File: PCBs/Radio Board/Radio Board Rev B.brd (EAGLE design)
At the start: 95.9 x 90.2 mm, 18 parts, among them J1 MOLEX_504050-0491, J1_1 TPTP10SQ, J1_2 TPTP10SQ, J1_3 TPTP10SQ, J1_4 TPTP10SQ

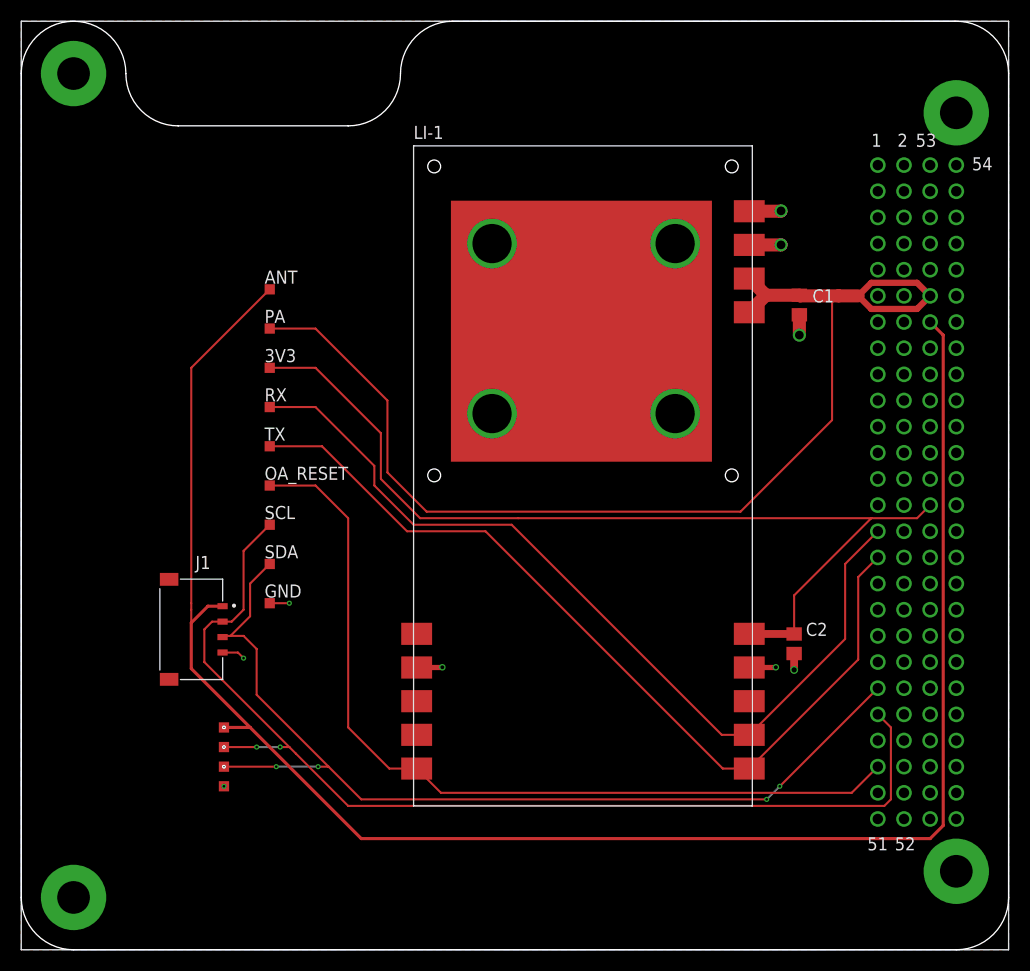
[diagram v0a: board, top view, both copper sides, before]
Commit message: Move MicroLock connector
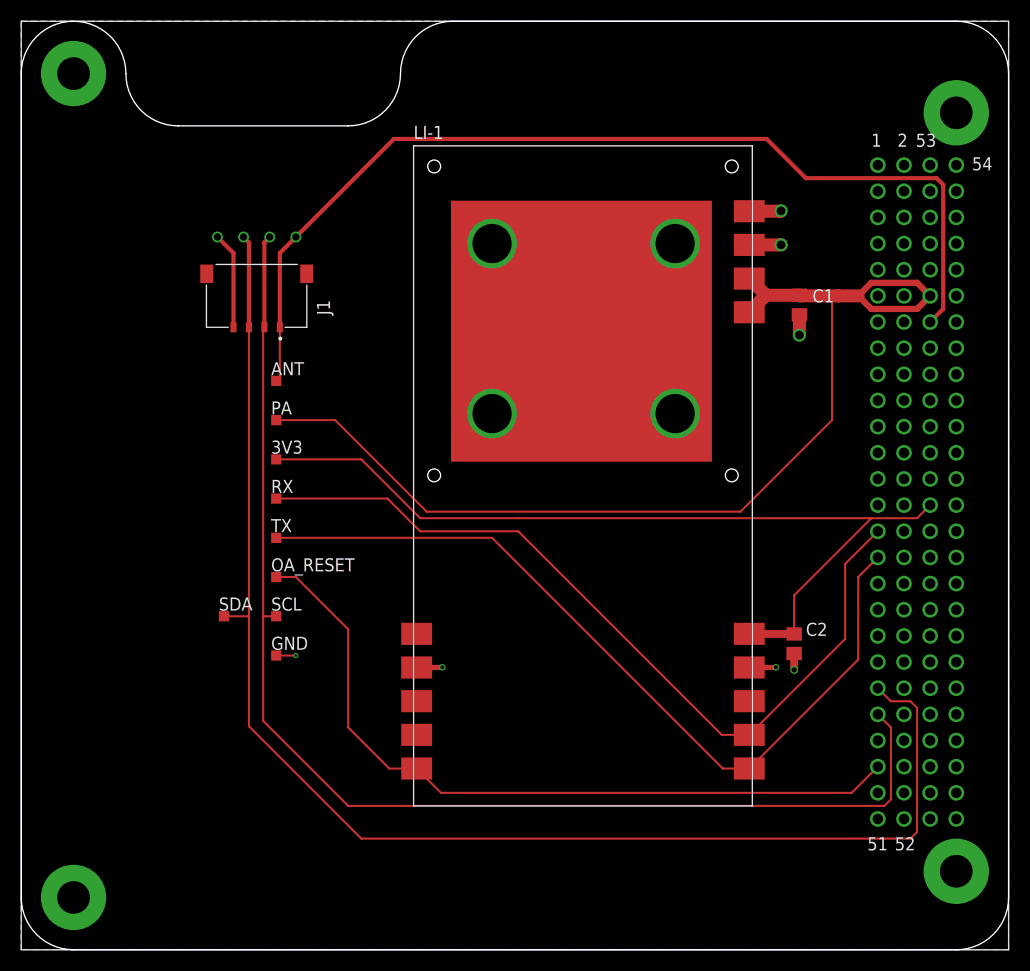
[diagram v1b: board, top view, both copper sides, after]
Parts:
- removed J1_1, J1_2, J1_3, J1_4: TPTP10SQ, testpad:TP10SQ
- moved J1 33.0 mm to (22.9, 63.5), turned to 180 degrees
- moved ANT 8.91 mm to (24.8, 55.2)
- moved 3V3 8.91 mm to (24.8, 47.6)
- moved OA_RESET 8.91 mm to (24.8, 36.2)
- moved PA 8.91 mm to (24.8, 51.4)
- moved RX 8.91 mm to (24.8, 43.8)
- moved SCL 8.91 mm to (24.8, 32.4)
- moved TX 8.91 mm to (24.8, 40.0)
- moved SDA 6.75 mm to (19.7, 32.4)
- moved GND 5.12 mm to (24.8, 28.6)
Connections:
- net GND: no longer J1_4.TP
- net SCL: no longer J1_2.TP
- net SDA: no longer J1_3.TP
- net SW5: no longer J1_1.TP
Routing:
- net SW5: track 176.0 -> 97.3 mm, vias 0 -> 1
- net SDA: track 96.1 -> 136.5 mm, vias 4 -> 1
- net SCL: track 104.9 -> 121.9 mm, vias 2 -> 1
- net OA_RESET: track 84.4 -> 73.7 mm
- net SW3: track 111.7 -> 103.3 mm
- net GND: track 19.0 -> 26.1 mm, vias 9 -> 8
- net 3V3: track 92.0 -> 85.1 mm
- net LI_RX: track 85.8 -> 80.4 mm
- net LI_TX: track 85.2 -> 80.9 mm

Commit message: Split I2C and SPI buses
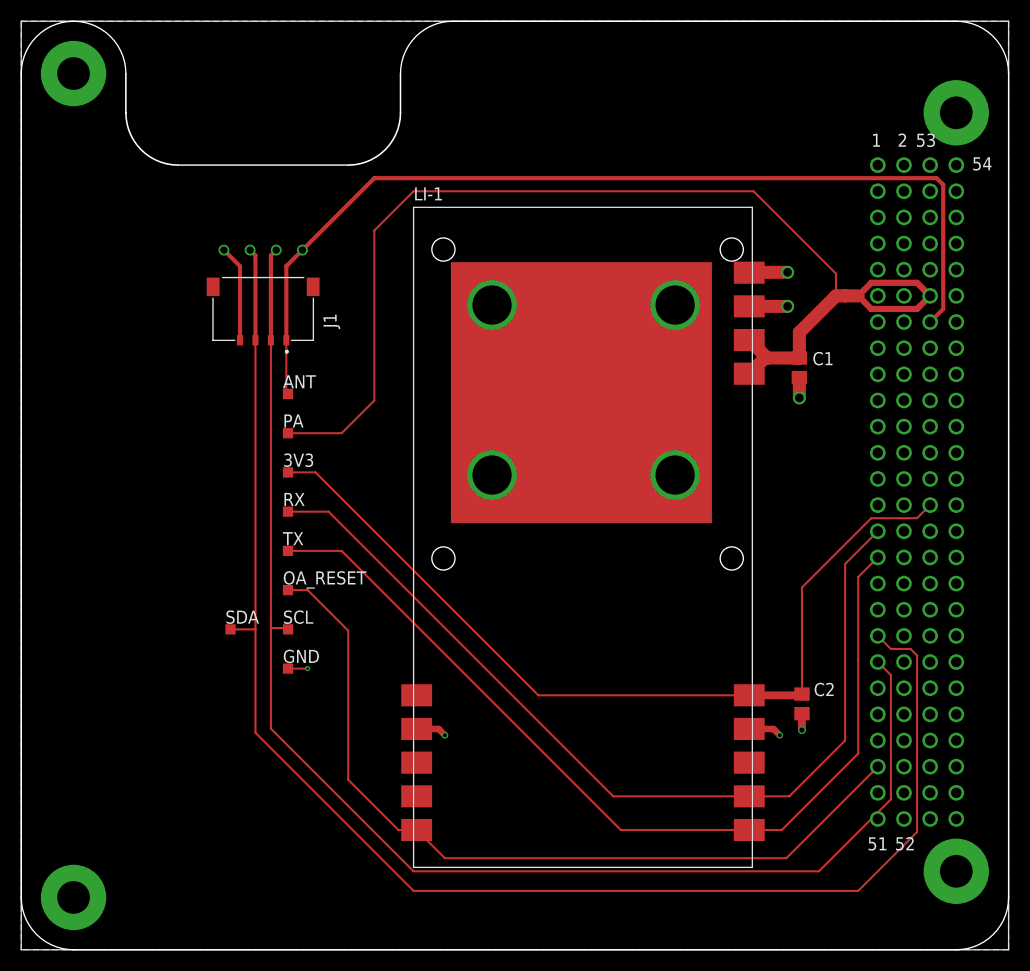
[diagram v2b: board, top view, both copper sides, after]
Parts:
- moved C1 6.10 mm to (75.6, 56.5)
- moved LI-1 5.97 mm to (38.1, 8.00)
- moved C2 5.89 mm to (75.8, 23.9)
- moved 3V3 1.71 mm to (25.9, 46.4)
- moved OA_RESET 1.71 mm to (25.9, 34.9)
- moved PA 1.71 mm to (25.9, 50.2)
- moved TX 1.71 mm to (25.9, 38.7)
- moved GND 1.71 mm to (25.9, 27.3)
- moved SCL 1.71 mm to (25.9, 31.1)
- moved ANT 1.71 mm to (25.9, 54.0)
- moved RX 1.71 mm to (25.9, 42.5)
- moved J1 1.42 mm to (23.5, 62.2)
- moved SDA 1.42 mm to (20.3, 31.1)
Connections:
- removed net SCL: J1.2, SCL.TP, U$1.43
- removed net SDA: J1.3, SDA.TP, U$1.41
- new net SCL_ANT: J1.2, SCL.TP, U$1.39
- new net SDA_ANT: J1.3, SDA.TP, U$1.37
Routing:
- net SDA_ANT: track 0.00 -> 144.2 mm, vias 0 -> 1
- net SDA: track 136.5 -> 0.00 mm, vias 1 -> 0
- net SCL_ANT: track 0.00 -> 131.1 mm, vias 0 -> 1
- net SCL: track 121.9 -> 0.00 mm, vias 1 -> 0
- net LI_RX: track 80.4 -> 89.4 mm
- net LI_TX: track 80.9 -> 89.5 mm
- net SW3: track 103.3 -> 111.9 mm
- net OA_RESET: track 73.7 -> 80.2 mm
- net SW5: track 97.3 -> 93.9 mm
- net GND: track 26.1 -> 28.5 mm
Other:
- outline, holes or cut-outs redrawn

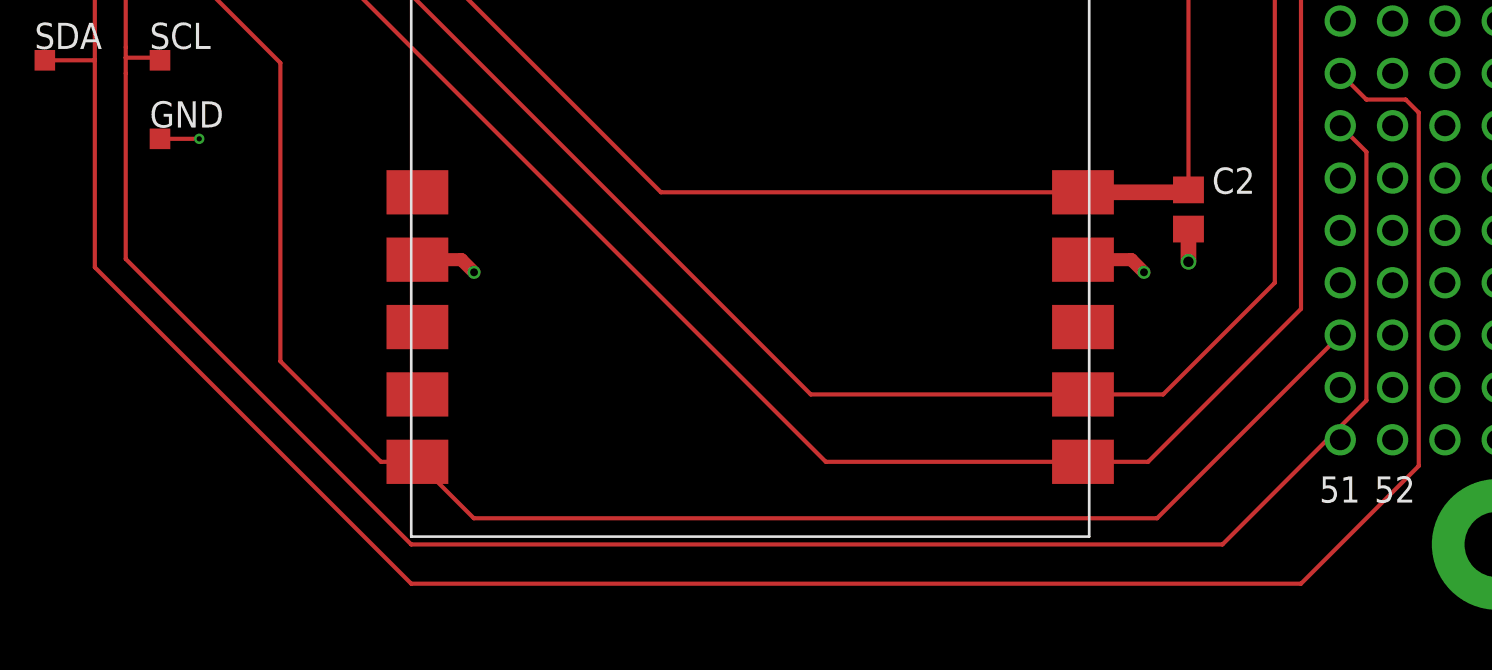
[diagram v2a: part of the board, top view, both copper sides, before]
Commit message: Fix trace collision
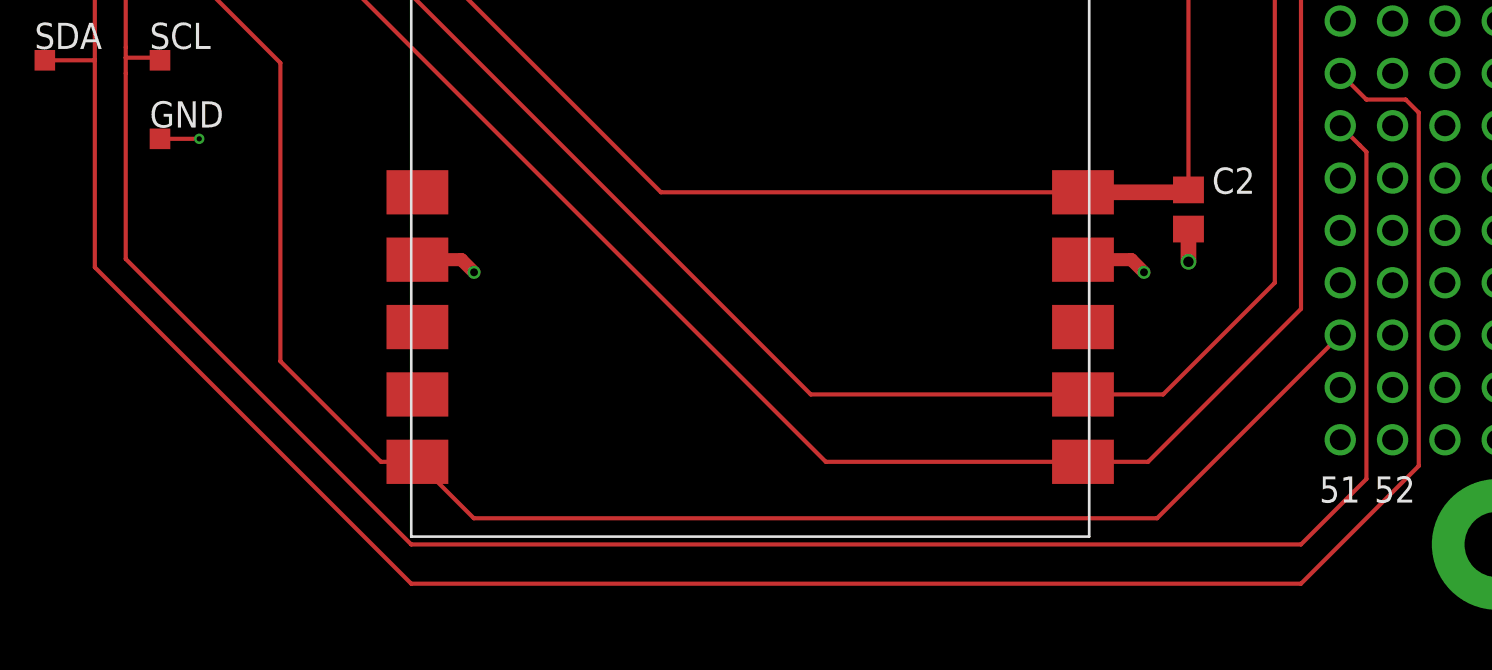
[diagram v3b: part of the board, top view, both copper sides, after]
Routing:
- net SCL_ANT: track 131.1 -> 133.3 mm
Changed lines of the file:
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@@
 <via x="24.765" y="67.945" extent="1-16" drill="0.7112"/>
 <contactref element="SCL" pad="TP"/>
-<wire x1="84.455" y1="14.605" x2="77.47" y2="7.62" width="0.2032" layer="1"/>
-<wire x1="38.1" y1="7.62" x2="77.47" y2="7.62" width="0.2032" layer="1"/>
 <contactref element="U$1" pad="39"/>
-<wire x1="83.185" y1="27.94" x2="84.455" y2="26.67" width="0.2032" layer="1"/>
-<wire x1="84.455" y1="26.67" x2="84.455" y2="14.605" width="0.2032" layer="1"/>
+<wire x1="83.185" y1="27.94" x2="84.1375" y2="26.9875" width="0.2032" layer="1"/>
+<wire x1="84.1375" y1="26.9875" x2="84.455" y2="26.67" width="0.2032" layer="1"/>
 <wire x1="24.245" y1="59.19" x2="24.245" y2="31.75" width="0.2032" layer="1"/>
 <wire x1="24.245" y1="31.75" x2="24.245" y2="31.242" width="0.2032" layer="1"/>
 <wire x1="24.245" y1="31.242" x2="24.245" y2="30.48" width="0.2032" layer="1"/>
 <wire x1="24.245" y1="30.48" x2="24.245" y2="21.475" width="0.2032" layer="1"/>
-<wire x1="24.245" y1="21.475" x2="38.1" y2="7.62" width="0.2032" layer="1"/>
+<wire x1="38.1" y1="7.62" x2="24.245" y2="21.475" width="0.2032" layer="1"/>
 <wire x1="25.908" y1="31.115" x2="25.781" y2="31.242" width="0.2032" layer="1"/>
 <wire x1="25.781" y1="31.242" x2="24.245" y2="31.242" width="0.2032" layer="1"/>
+<wire x1="84.455" y1="26.67" x2="84.455" y2="10.795" width="0.2032" layer="1"/>
+<wire x1="84.455" y1="10.795" x2="81.28" y2="7.62" width="0.2032" layer="1"/>
+<wire x1="81.28" y1="7.62" x2="38.1" y2="7.62" width="0.2032" layer="1"/>
 </signal>
 <signal name="SDA_ANT">

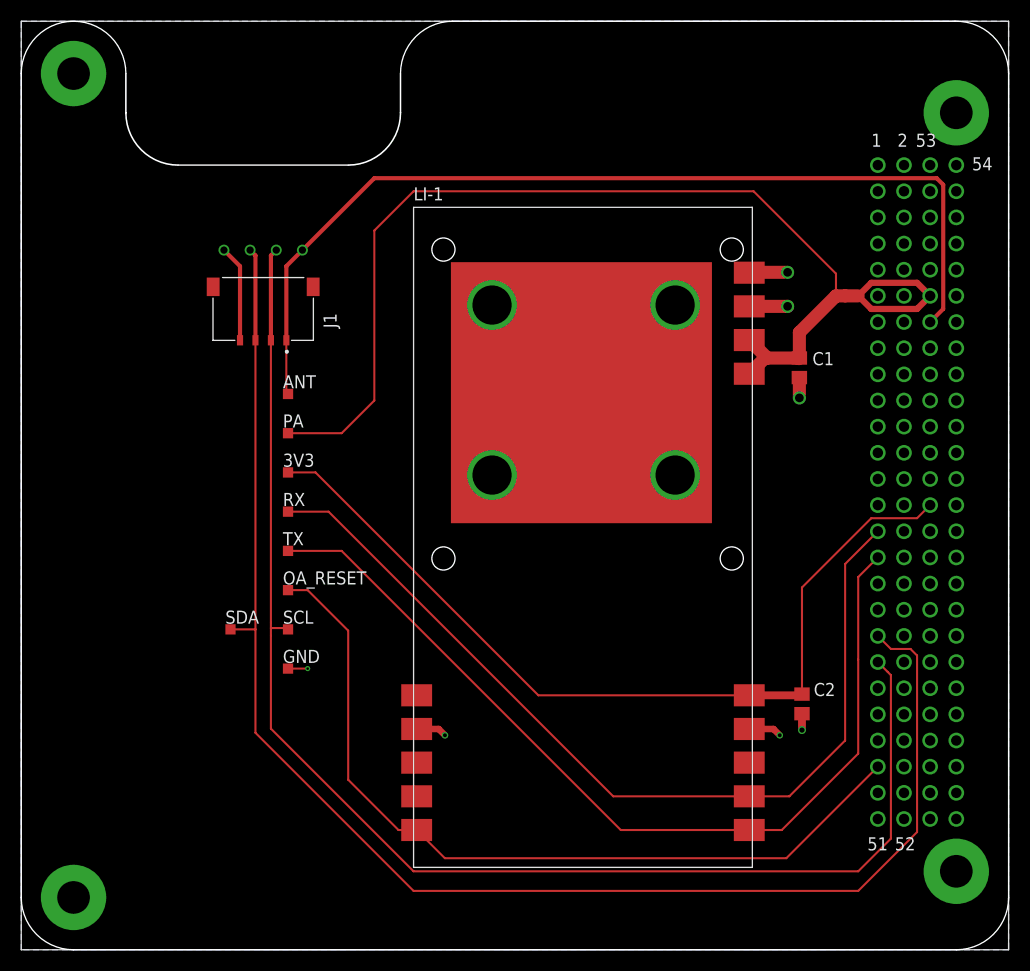
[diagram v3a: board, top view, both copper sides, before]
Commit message: Improve decoupling, ground impedance, silkscreens
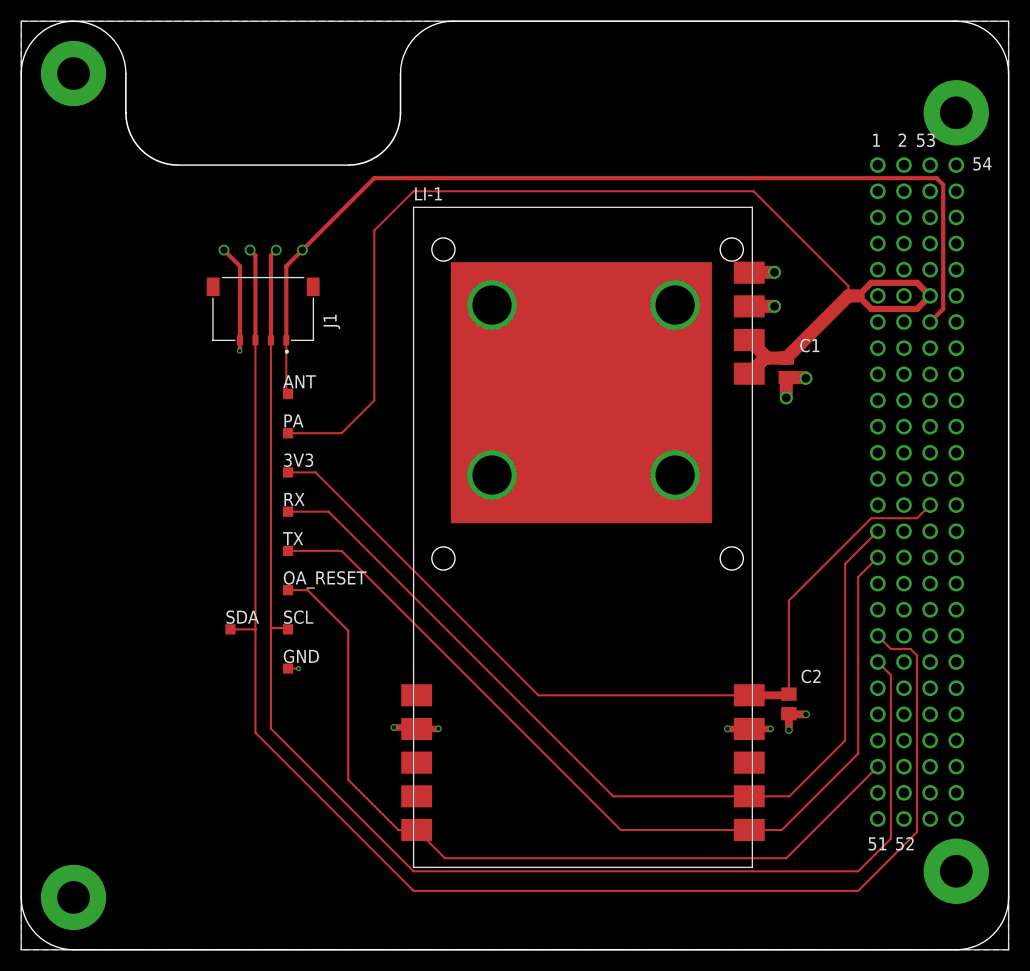
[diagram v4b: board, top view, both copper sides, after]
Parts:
- moved C1 1.27 mm to (74.3, 56.5)
- moved C2 1.27 mm to (74.5, 23.9)
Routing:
- net GND: track 28.5 -> 32.1 mm, vias 8 -> 13
- net SW3: track 111.9 -> 110.8 mm
- net 3V3: track 85.0 -> 84.3 mm
